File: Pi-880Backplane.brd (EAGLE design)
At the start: 105.4 x 71.1 mm, 2 parts

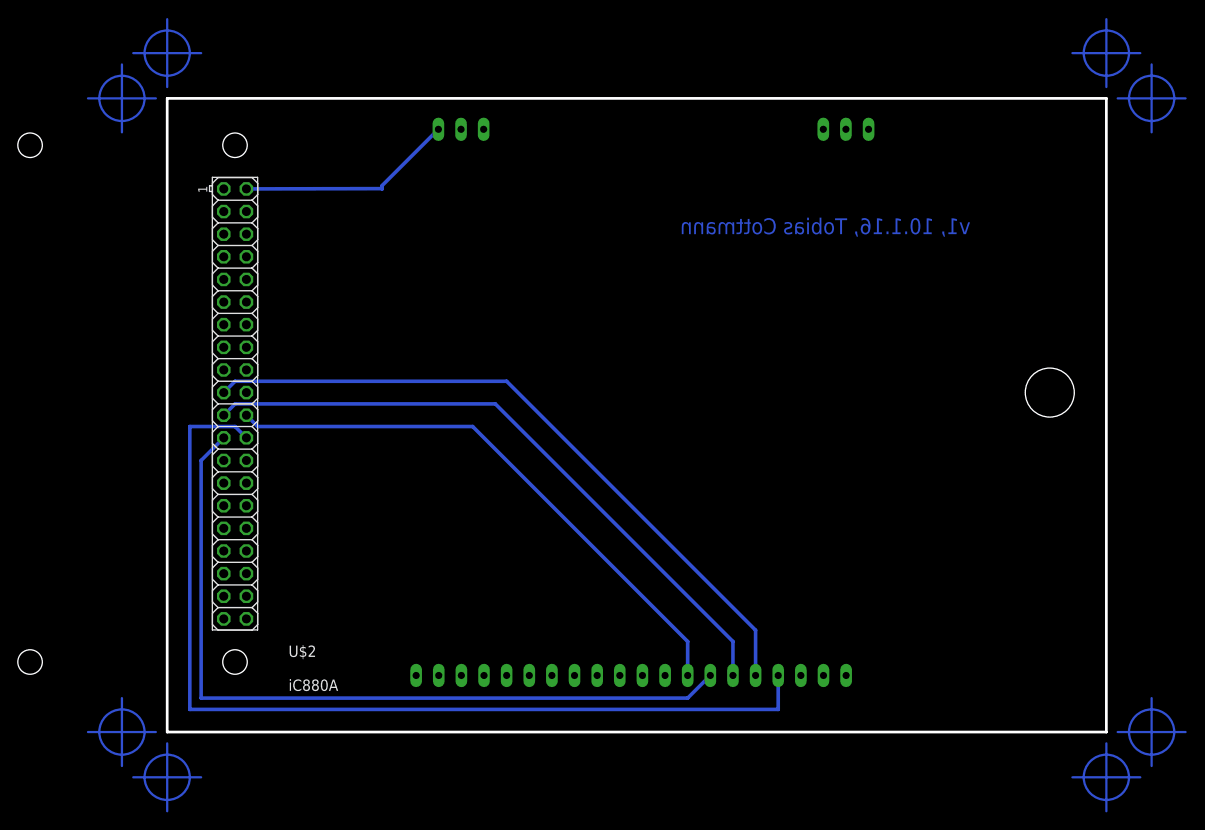
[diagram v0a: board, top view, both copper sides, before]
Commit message: Drill holes bigger
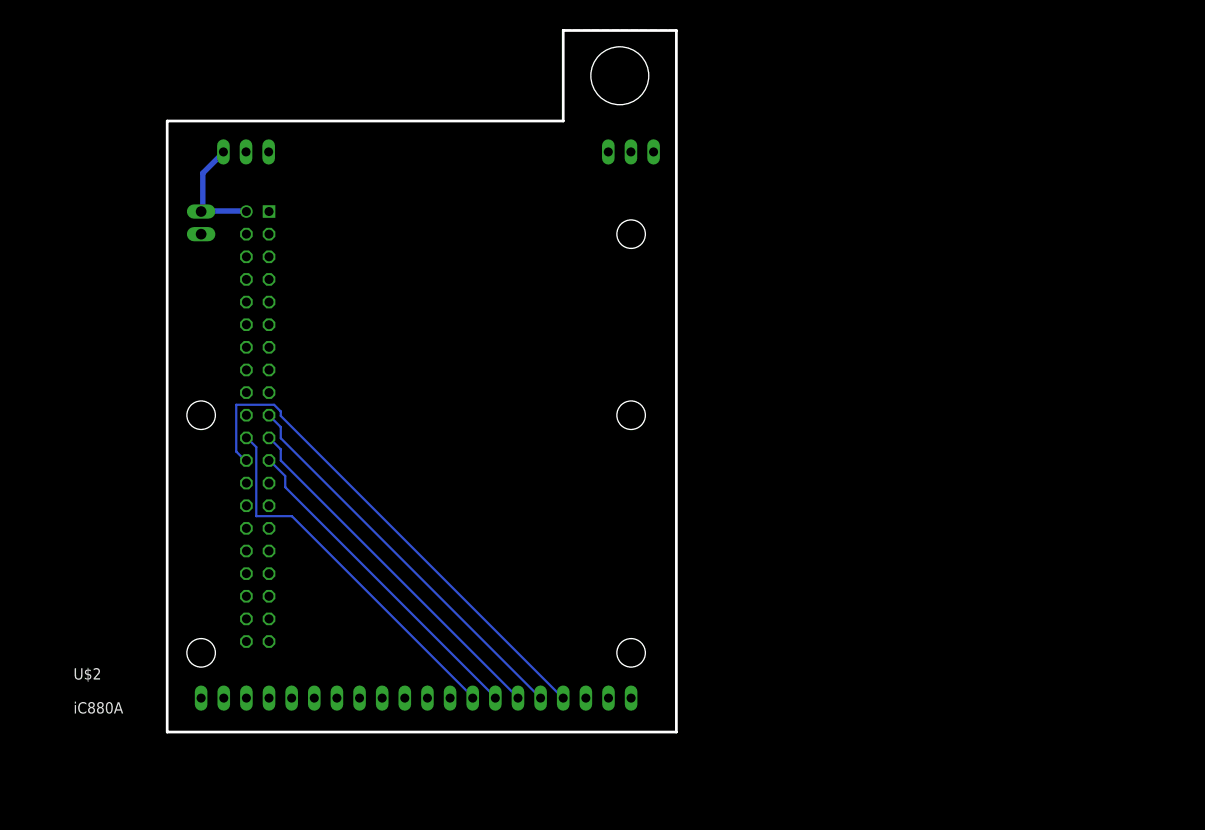
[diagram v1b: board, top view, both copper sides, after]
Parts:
- added X1: (no value), con-phoenix-254:2POL254
- U$1: value RPI-ZERO -> RPI-ZERONODRILLS; device RPI-Zero:RASPBERRYPI_BASTELSTUBE_V13_RASPI_BOARD_B+_FULL -> tobias:RPI-ZERO-NODRILLS
- moved U$1 55.9 mm to (36.8, 67.3), flipped to the bottom
- moved U$2 24.3 mm to (-12.7, 0.00)
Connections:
- net GND: now also X1.2
- net VCC: now also X1.1
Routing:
- net SPI_CLK: track 88.5 -> 37.2 mm
- net NSS: track 108.5 -> 57.4 mm
- net MOSI: track 76.9 -> 44.4 mm
- net MISO: track 72.5 -> 40.8 mm
- net RESET: track 63.9 -> 42.1 mm
- net VCC: track 24.6 -> 12.7 mm
- net N$6: track 7.62 -> 0.00 mm
- net N$2: track 7.62 -> 0.00 mm
- net N$16: track 7.62 -> 0.00 mm
- net N$13: track 7.62 -> 0.00 mm
- net N$12: track 7.62 -> 0.00 mm
- net N$11: track 7.62 -> 0.00 mm
- net N$3: track 7.62 -> 0.00 mm
- net N$14: track 7.62 -> 0.00 mm
- net N$10: track 7.62 -> 0.00 mm
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- added copper zone on layer 1, net GND
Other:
- board size 105.4 x 71.1 mm -> 57.1 x 78.7 mm
- board text removed: "v1, 10.1.16, Tobias Cottmann"

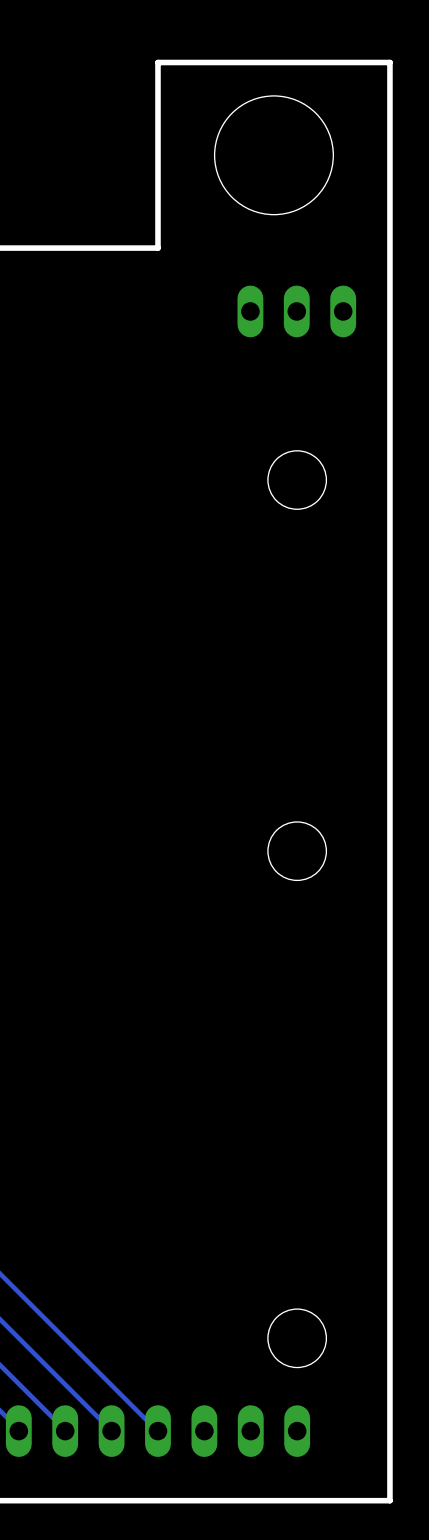
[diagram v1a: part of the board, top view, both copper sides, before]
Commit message: Better SMA mount
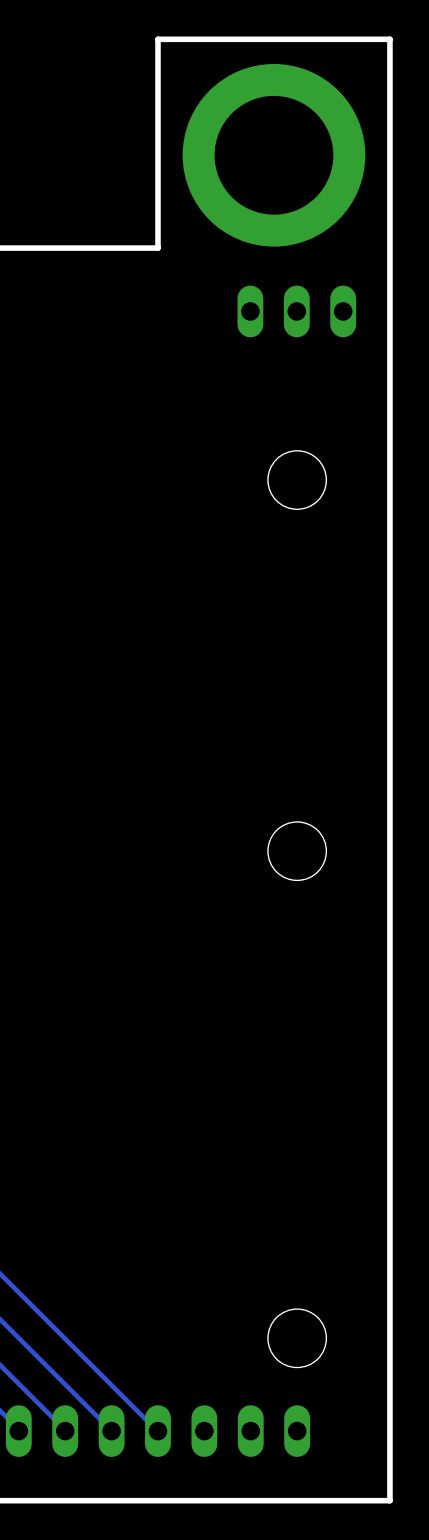
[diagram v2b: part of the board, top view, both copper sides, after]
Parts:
- added U$3: SMA-PIGTAIL-MOUNT, tobias:SMA-PIGTAIL-MOUNT
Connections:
- net GND: now also U$3.GND
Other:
- board size 57.1 x 78.7 mm -> 57.1 x 80 mm
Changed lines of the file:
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@@
 <wire x1="0" y1="0" x2="0" y2="68.58" width="0.3048" layer="20"/>
 <wire x1="0" y1="68.58" x2="44.45" y2="68.58" width="0.3048" layer="20"/>
-<wire x1="44.45" y1="68.58" x2="44.45" y2="78.74" width="0.3048" layer="20"/>
-<wire x1="44.45" y1="78.74" x2="57.15" y2="78.74" width="0.3048" layer="20"/>
-<wire x1="57.15" y1="78.74" x2="57.15" y2="0" width="0.3048" layer="20"/>
+<wire x1="44.45" y1="68.58" x2="44.45" y2="80.01" width="0.3048" layer="20"/>
+<wire x1="44.45" y1="80.01" x2="57.15" y2="80.01" width="0.3048" layer="20"/>
+<wire x1="57.15" y1="80.01" x2="57.15" y2="0" width="0.3048" layer="20"/>
 <wire x1="57.15" y1="0" x2="0" y2="0" width="0.3048" layer="20"/>
-<hole x="50.8" y="73.66" drill="6.5"/>
 <hole x="52.07" y="55.88" drill="3.2"/>
 <hole x="52.07" y="8.89" drill="3.2"/>
@@
 <hole x="52.07" y="35.56" drill="3.2"/>
 <wire x1="0" y1="68.58" x2="44.45" y2="68.58" width="0" layer="46"/>
-<wire x1="44.45" y1="68.58" x2="44.45" y2="78.74" width="0" layer="46"/>
-<wire x1="44.45" y1="78.74" x2="57.15" y2="78.74" width="0" layer="46"/>
-<wire x1="57.15" y1="78.74" x2="57.15" y2="0" width="0" layer="46"/>
+<wire x1="44.45" y1="68.58" x2="44.45" y2="80.01" width="0" layer="46"/>
+<wire x1="44.45" y1="80.01" x2="57.15" y2="80.01" width="0" layer="46"/>
+<wire x1="57.15" y1="80.01" x2="57.15" y2="0" width="0" layer="46"/>
 <wire x1="57.15" y1="0" x2="0" y2="0" width="0" layer="46"/>
 <wire x1="0" y1="0" x2="0" y2="68.58" width="0" layer="46"/>
@@
 <attribute name="MF" value="" x="3.81" y="57.15" size="1.778" layer="28" rot="MR270" display="off"/>
 </element>
+<element name="U$3" library="tobias" package="SMA-PIGTAIL-MOUNT" value="SMA-PIGTAIL-MOUNT" x="50.8" y="73.66"/>
 </elements>
 <signals>
@@
 <vertex x="0" y="0"/>
 <vertex x="57.15" y="0"/>
-<vertex x="57.15" y="78.74"/>
-<vertex x="44.45" y="78.74"/>
+<vertex x="57.15" y="80.01"/>
+<vertex x="44.45" y="80.01"/>
 <vertex x="44.45" y="68.58"/>
 <vertex x="0" y="68.58"/>
@@
 <vertex x="0" y="68.58"/>
 <vertex x="44.45" y="68.58"/>
-<vertex x="44.45" y="78.74"/>
-<vertex x="57.15" y="78.74"/>
+<vertex x="44.45" y="80.01"/>
+<vertex x="57.15" y="80.01"/>
 <vertex x="57.15" y="0"/>
 <vertex x="0" y="0"/>
 </polygon>
 <contactref element="X1" pad="2"/>
+<contactref element="U$3" pad="GND"/>
 </signal>
 <signal name="RESET">
